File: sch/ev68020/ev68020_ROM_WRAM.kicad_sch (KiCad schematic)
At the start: 17 parts, among them SW4 ROM Bank Sel., U24 29F002, U25 CY7C185, U26 CY7C185, U27 CY7C185, U28 CY7C185, U29 HM62256BLP

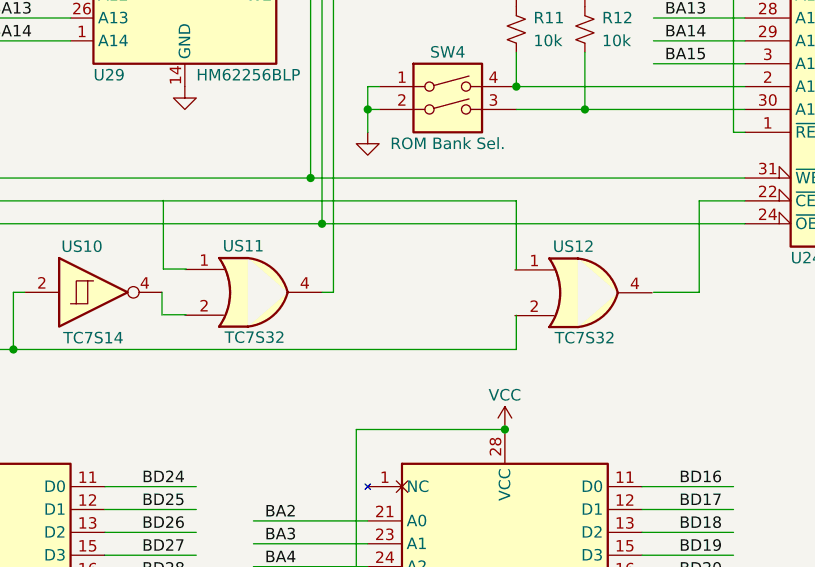
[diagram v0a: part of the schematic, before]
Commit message: minimal fix: change wire attributes
change RAS/CASH/CASL
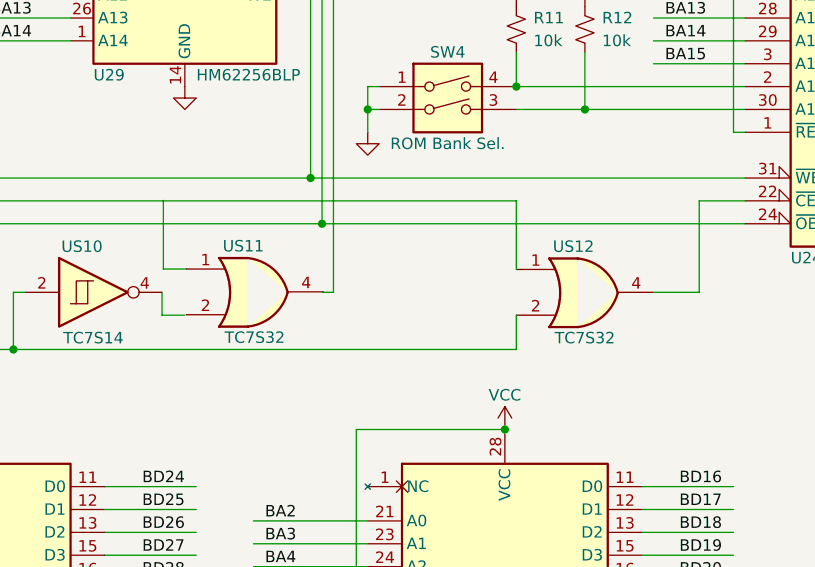
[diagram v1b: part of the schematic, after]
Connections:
- net CS_ROM*: now also US12.2
- net SEL_0*: now also US12.1
- net at US12.4: now also U24.22 (~{CE})
- net at U29.20 (~{CS}): no longer US11.4
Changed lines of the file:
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@@
+    (stroke (width 0) (type default) (color 0 0 0 0))
+  )
+  (wire (pts (xy 74.93 100.33) (xy 77.47 100.33))
     (stroke (width 0) (type default) (color 0 0 0 0))
   )
@@
   )
   (wire (pts (xy 78.74 127) (xy 68.58 127))
-    (stroke (width 0) (type default) (color 0 0 0 0))
-  )
-  (wire (pts (xy 75.0826 100.2792) (xy 77.6226 100.2792))
     (stroke (width 0) (type default) (color 0 0 0 0))
   )
@@
     (pin "9")
   )
-  (symbol (lib_id "Toshiba_Sp:TC7S32") (at 83.9726 97.7392 0) (unit 1)
+  (symbol (lib_name "TC7S32_1") (lib_id "Toshiba_Sp:TC7S32") (at 83.9726 97.7392 0) (unit 1)
     (in_bom yes) (on_board yes)
     (property "Reference" "US11" (id 0) (at 83.9726 92.6592 0))
